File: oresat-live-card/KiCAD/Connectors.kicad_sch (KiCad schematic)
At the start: 31 parts, among them J1 ORESAT-DEBUG-CONNECTOR-CARD, J4 TFM-120-01-L-D-RA, J6 J-MOLEX-SMPM-73300-003X

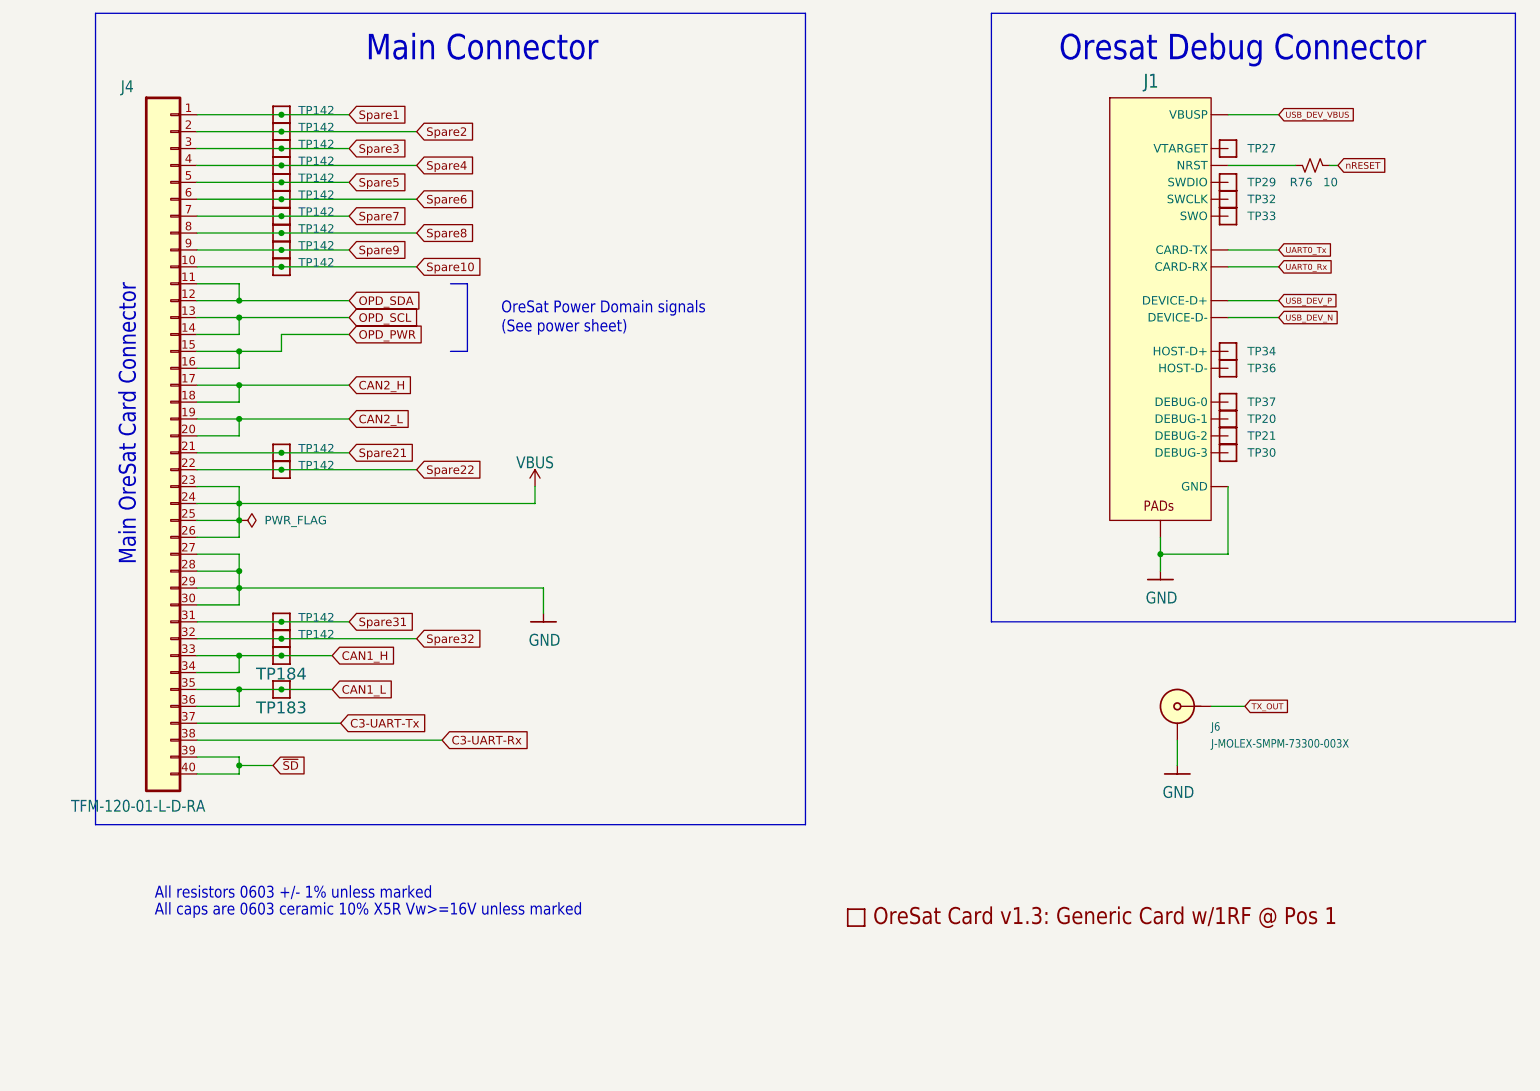
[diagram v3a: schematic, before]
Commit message: added new sheets for LNA and switching
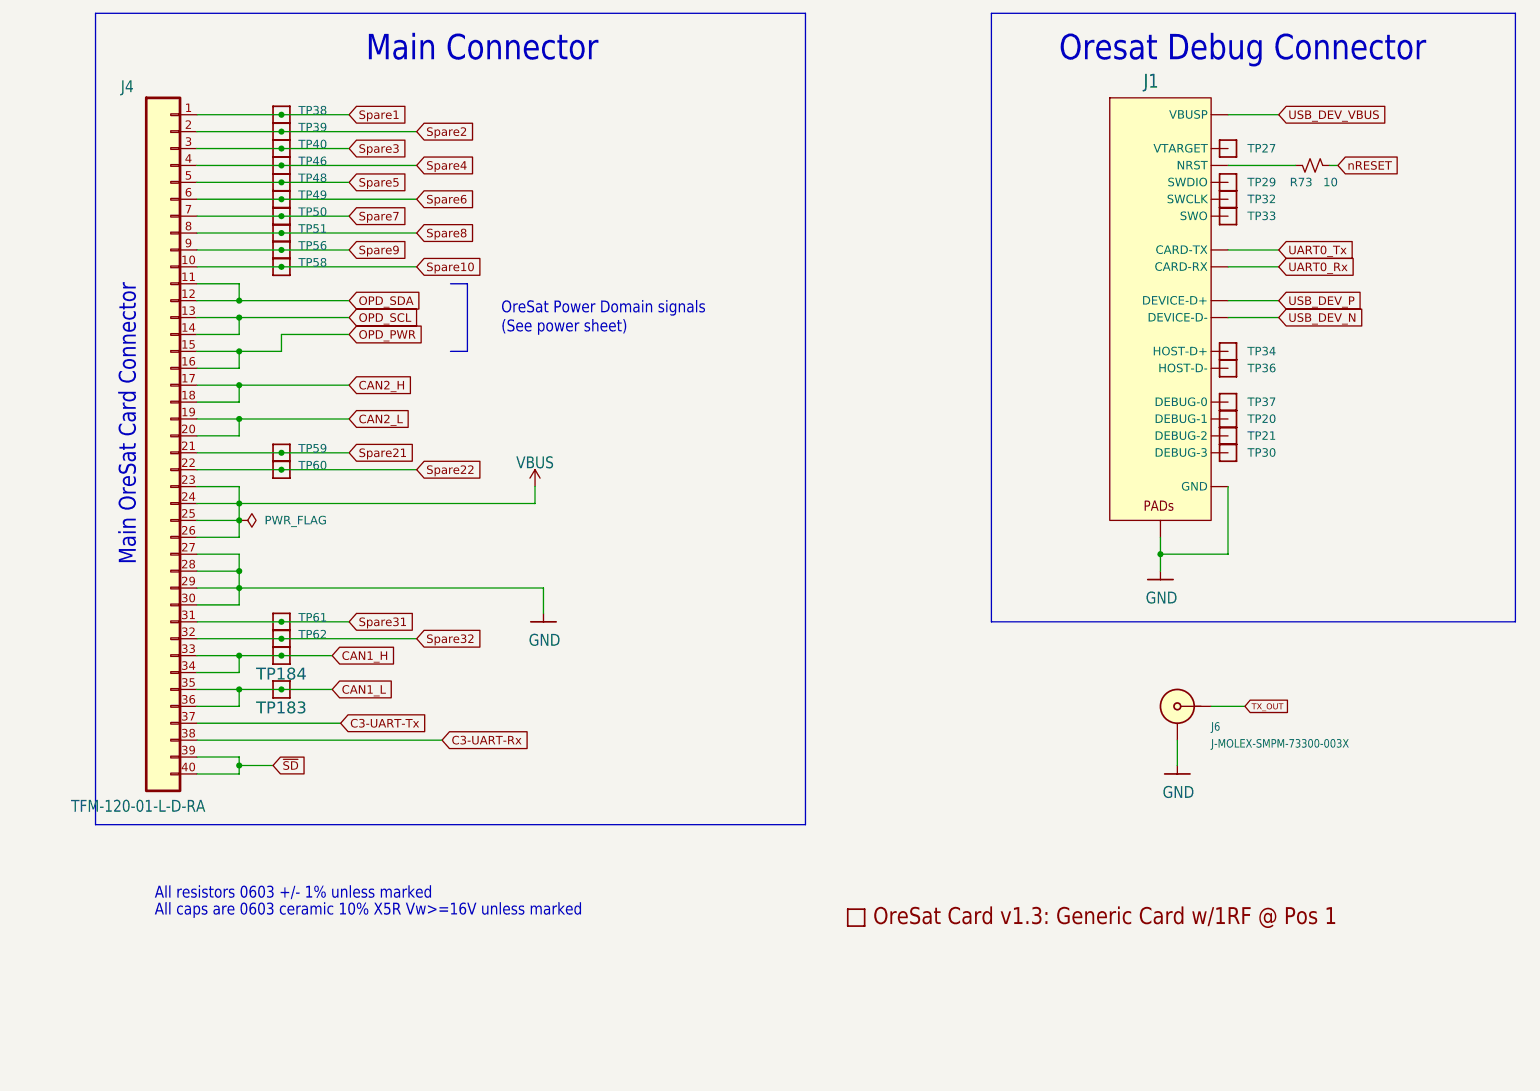
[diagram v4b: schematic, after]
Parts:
- renumbered R76 to R73, TP142 to TP38, TP142 to TP39, TP142 to TP40, TP142 to TP46, TP142 to TP48, TP142 to TP49, TP142 to TP50, TP142 to TP51, TP142 to TP56, TP142 to TP58, TP142 to TP59, TP142 to TP60, TP142 to TP61, TP142 to TP62
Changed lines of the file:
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@@
 (kicad_sch
-	(version 20231120)
+	(version 20250114)
 	(generator "eeschema")
-	(generator_version "8.0")
+	(generator_version "9.0")
 	(paper "B")
 	(title_block
@@
 		(rev "1.3")
 	)
+	(text "OreSat Power Domain signals\n(See power sheet)"
+		(exclude_from_sim no)
+		(at 177.8 109.22 0)
+		(effects
+			(font
+				(size 1.778 1.5113)
+			)
+			(justify left bottom)
+		)
+	)
+	(text "All resistors 0603 +/- 1% unless marked"
+		(exclude_from_sim no)
+		(at 125.73 194.31 0)
+		(effects
+			(font
+				(size 1.778 1.5113)
+			)
+			(justify left bottom)
+		)
+	)
+	(text "Main Connector"
+		(exclude_from_sim no)
+		(at 157.48 68.58 0)
+		(effects
+			(font
+				(size 3.81 3.2385)
+			)
+			(justify left bottom)
+		)
+	)
+	(text "Main OreSat Card Connector"
+		(exclude_from_sim no)
+		(at 123.19 101.6 90)
+		(effects
+			(font
+				(size 2.54 2.159)
+			)
+			(justify right bottom)
+		)
+	)
+	(text "All caps are 0603 ceramic 10% X5R Vw>=16V unless marked"
+		(exclude_from_sim no)
+		(at 125.73 196.85 0)
+		(effects
+			(font
+				(size 1.778 1.5113)
+			)
+			(justify left bottom)
+		)
+	)
+	(text "Oresat Debug Connector"
+		(exclude_from_sim no)
+		(at 261.62 68.58 0)
+		(effects
+			(font
+				(size 3.81 3.2385)
+			)
+			(justify left bottom)
+		)
+	)
 	(junction
 		(at 138.43 106.68)
@@
 		)
 	)
-	(text "OreSat Power Domain signals\n(See power sheet)"
-		(exclude_from_sim no)
-		(at 177.8 109.22 0)
-		(effects
-			(font
-				(size 1.778 1.5113)
-			)
-			(justify left bottom)
-		)
-	)
-	(text "All resistors 0603 +/- 1% unless marked"
-		(exclude_from_sim no)
-		(at 125.73 194.31 0)
-		(effects
-			(font
-				(size 1.778 1.5113)
-			)
-			(justify left bottom)
-		)
-	)
-	(text "Main Connector"
-		(exclude_from_sim no)
-		(at 157.48 68.58 0)
-		(effects
-			(font
-				(size 3.81 3.2385)
-			)
-			(justify left bottom)
-		)
-	)
-	(text "Main OreSat Card Connector"
-		(exclude_from_sim no)
-		(at 123.19 101.6 90)
-		(effects
-			(font
-				(size 2.54 2.159)
-			)
-			(justify right bottom)
-		)
-	)
-	(text "All caps are 0603 ceramic 10% X5R Vw>=16V unless marked"
-		(exclude_from_sim no)
-		(at 125.73 196.85 0)
-		(effects
-			(font
-				(size 1.778 1.5113)
-			)
-			(justify left bottom)
-		)
-	)
-	(text "Oresat Debug Connector"
-		(exclude_from_sim no)
-		(at 261.62 68.58 0)
-		(effects
-			(font
-				(size 3.81 3.2385)
-			)
-			(justify left bottom)
-		)
-	)
 	(global_label "UART0_Rx"
 		(shape input)
@@
 		(effects
 			(font
-				(size 0.889 0.889)
+				(size 1.27 1.27)
 			)
 			(justify left)
 		)
 		(property "Intersheetrefs" "${INTERSHEET_REFS}"
-			(at 303.1218 99.06 0)
+			(at 306.7571 99.06 0)
 			(effects
 				(font
@@
 		(effects
 			(font
-				(size 0.889 0.889)
+				(size 1.27 1.27)
 			)
 			(justify left)
 		)
 		(property "Intersheetrefs" "${INTERSHEET_REFS}"
-			(at 306.6354 76.2 0)
+			(at 311.7766 76.2 0)
 			(effects
 				(font
@@
 		(effects
 			(font
-				(size 0.889 0.889)
+				(size 1.27 1.27)
 			)
 			(justify left)
 		)
 		(property "Intersheetrefs" "${INTERSHEET_REFS}"
-			(at 302.9101 96.52 0)
+			(at 306.4547 96.52 0)
 			(effects
 				(font
@@
 		(effects
 			(font
-				(size 0.889 0.889)
+				(size 1.27 1.27)
 			)
 			(justify left)
 		)
 		(property "Intersheetrefs" "${INTERSHEET_REFS}"
-			(at 304.0954 104.14 0)
+			(at 308.148 104.14 0)
 			(effects
 				(font
@@
 		(effects
 			(font
-				(size 1 1)
+				(size 1.27 1.27)
 			)
 			(justify left)
 		)
 		(property "Intersheetrefs" "${INTERSHEET_REFS}"
-			(at 311.309 83.82 0)
+			(at 313.4093 83.82 0)
 			(effects
 				(font
@@
 		(effects
 			(font
-				(size 0.889 0.889)
+				(size 1.27 1.27)
 			)
 			(justify left)
 		)
 		(property "Intersheetrefs" "${INTERSHEET_REFS}"
-			(at 304.1377 106.68 0)
+			(at 308.2085 106.68 0)
 			(effects
 				(font
@@
 		(on_board yes)
 		(dnp no)
-		(property "Reference" "TP142"
+		(property "Reference" "TP48"
 			(at 147.32 85.725 90)
 			(effects
@@
 		(dnp no)
 		(fields_autoplaced yes)
-		(property "Reference" "#FLG02"
+		(property "Reference" "#FLG01"
 			(at 140.335 137.16 0)
 			(effects
@@
 		(on_board yes)
 		(dnp no)
-		(property "Reference" "TP142"
+		(property "Reference" "TP46"
 			(at 147.32 83.185 90)
 			(effects
@@
 		(on_board yes)
 		(dnp no)
-		(property "Reference" "R76"
+		(property "Reference" "R73"
 			(at 299.72 86.36 90)
 			(effects
@@
 		(on_board yes)
 		(dnp no)
-		(property "Reference" "TP142"
+		(property "Reference" "TP40"
 			(at 147.32 80.645 90)
 			(effects
@@
 		(on_board yes)
 		(dnp no)
-		(property "Reference" "TP142"
+		(property "Reference" "TP61"
 			(at 147.32 151.765 90)
 			(effects
@@
 		(on_board yes)
 		(dnp no)
-		(property "Reference" "TP142"
+		(property "Reference" "TP50"
 			(at 147.32 90.805 90)
 			(effects
@@
 		(on_board yes)
 		(dnp no)
-		(property "Reference" "TP142"
+		(property "Reference" "TP39"
 			(at 147.32 78.105 90)
 			(effects
@@
 		(on_board yes)
 		(dnp no)
-		(property "Reference" "TP142"
+		(property "Reference" "TP56"
 			(at 147.32 95.885 90)
 			(effects
@@
 		(on_board yes)
 		(dnp no)
-		(property "Reference" "TP142"
+		(property "Reference" "TP60"
 			(at 147.32 128.905 90)
 			(effects
@@
 		(on_board yes)
 		(dnp no)
-		(property "Reference" "TP142"
+		(property "Reference" "TP59"
 			(at 147.32 126.365 90)
 			(effects
@@
 		(on_board yes)
 		(dnp no)
-		(property "Reference" "TP142"
+		(property "Reference" "TP62"
 			(at 147.32 154.305 90)
 			(effects
@@
 		(on_board yes)
 		(dnp no)
-		(property "Reference" "TP142"
+		(property "Reference" "TP58"
 			(at 147.32 98.425 90)
 			(effects
@@
 		(on_board yes)
 		(dnp no)
-		(property "Reference" "TP142"
+		(property "Reference" "TP38"
 			(at 147.32 75.565 90)
 			(effects
@@
 		(on_board yes)
 		(dnp no)
-		(property "Reference" "TP142"
+		(property "Reference" "TP49"
 			(at 147.32 88.265 90)
 			(effects
@@
 		(on_board yes)
 		(dnp no)
-		(property "Reference" "TP142"
+		(property "Reference" "TP51"
 			(at 147.32 93.345 90)
 			(effects

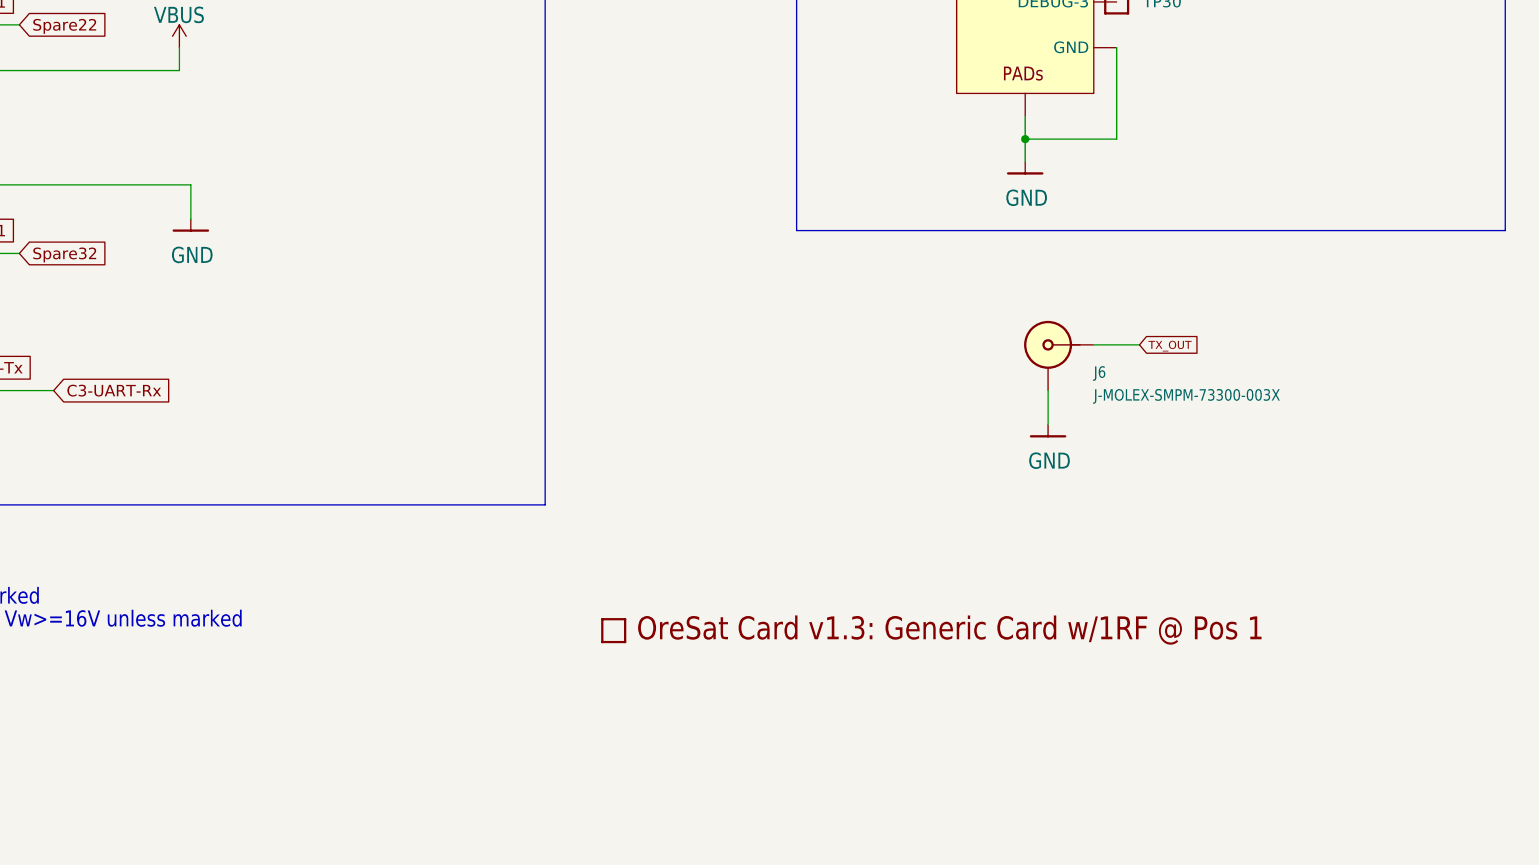
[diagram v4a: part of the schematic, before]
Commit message: completed tx/rx switch circuit and cleaned up GND references
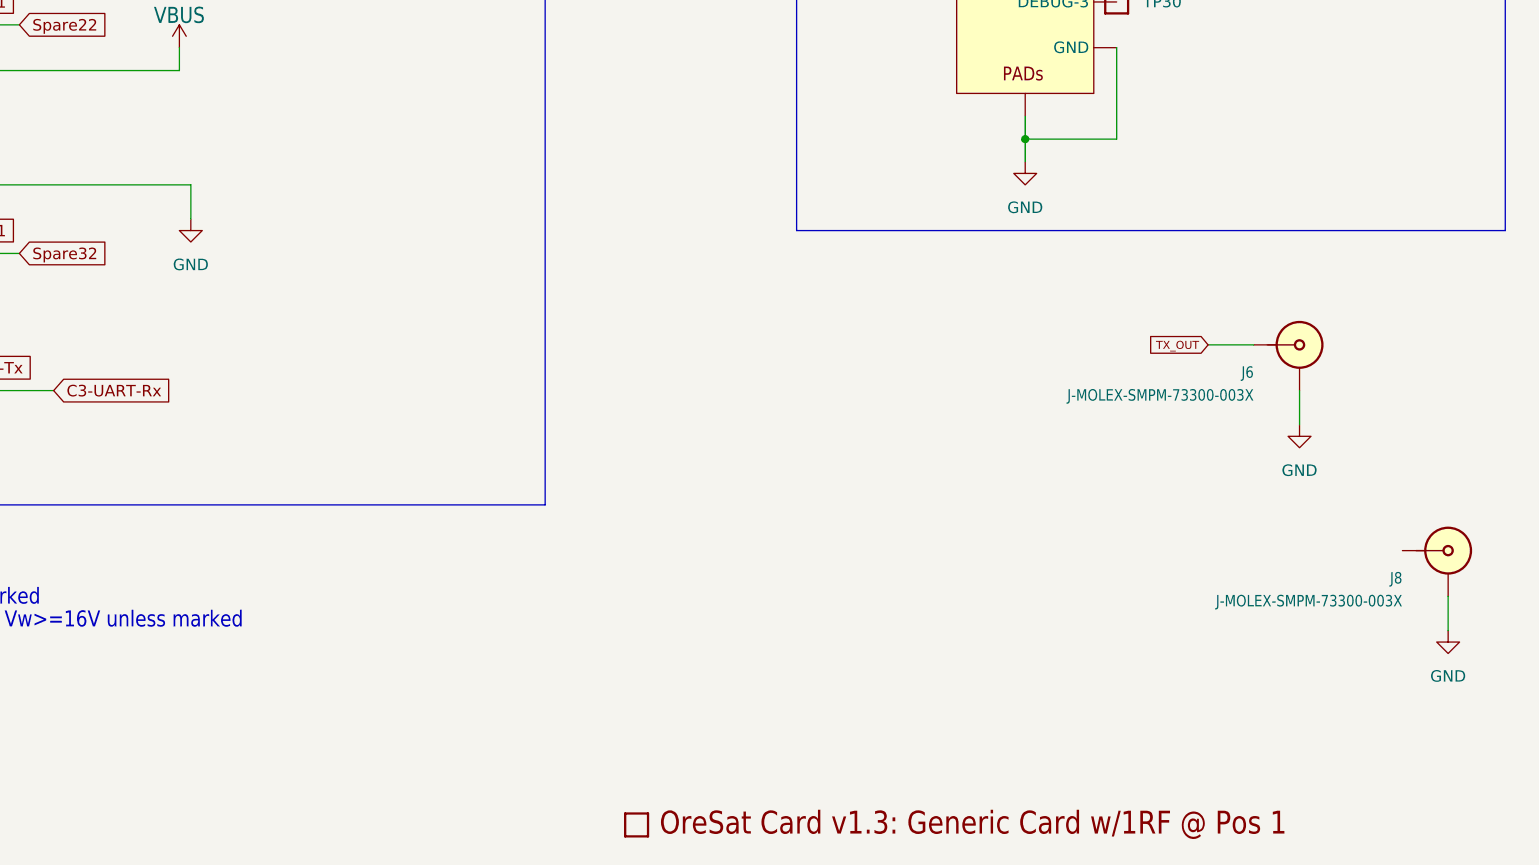
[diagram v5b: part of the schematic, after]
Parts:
- added J8: J-MOLEX-SMPM-73300-003X, oresat-connectors:J-MOLEX-SMPM-073300-002X, symbol oresat-connectors:J-MOLEX-SMPM-73300-002X
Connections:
- net GND: now also J8.SHLD
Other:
- moved on the sheet: J6
